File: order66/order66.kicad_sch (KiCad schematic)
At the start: 214 parts, among them J1 NICEVIEW, J2 Pouch Battery Connector, J3 swd connector, J4 3220-10-0100-00, J6 millmax connector, SW1 AUX1, SW10 Z, SW100 OFF/ON, SW11 AUX7, SW12 2, SW13 W, SW14 S, SW15 X, SW16 LALT, SW17 3, SW18 E, SW19 D, SW2 ESC, SW20 C, SW21 GUI, SW22 4, SW23 R, SW24 F, SW25 V, SW26 RAISE, SW27 5, SW28 T, SW29 G, SW3 TAB, SW30 B, SW31 LSPACE, SW32 AUX2, SW33 6, SW34 Y, SW35 H, SW36 N, SW37 RSPACE, SW38 AUX3, SW39 7, SW4 CAPSLCK, SW40 U, SW41 J, SW42 M, SW43 LOWER, SW44 AUX4, SW45 8, SW46 I, SW47 K, SW48 ,<, SW49 LEFT, SW5 LSHIFT, SW50 9, SW51 O, SW52 L, SW53 .>, SW54 DOWN, SW55 AUX5, SW56 0, SW57 P, SW58 ;:, SW59 /?, SW6 LCTRL, SW60 UP, SW61 AUX6, SW62 BACKSPACE, SW63 BACKSLASH, SW64 ENTER, SW65 RSHIFT, SW66 RIGHT, SW67 RST, SW68 OFF/ON, SW7 1, SW8 Q, SW9 A, U1 NiceNano

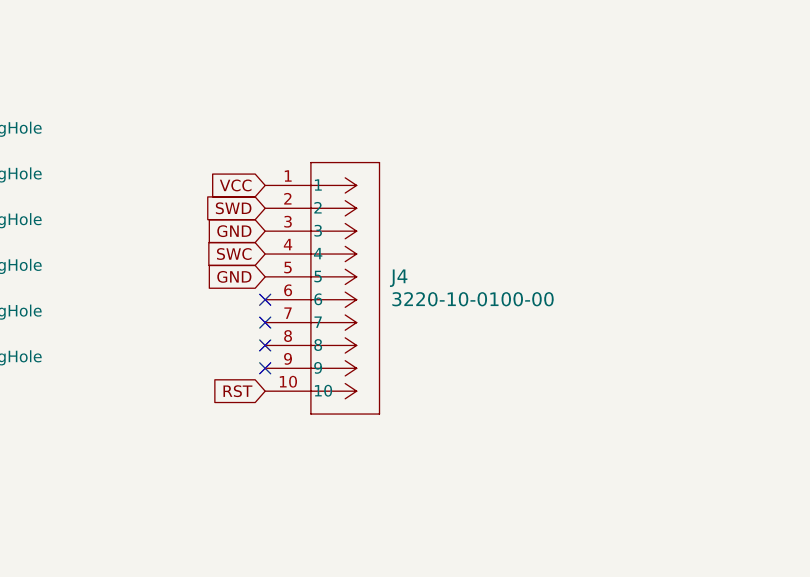
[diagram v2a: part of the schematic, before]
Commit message: removing the connector for the link for now
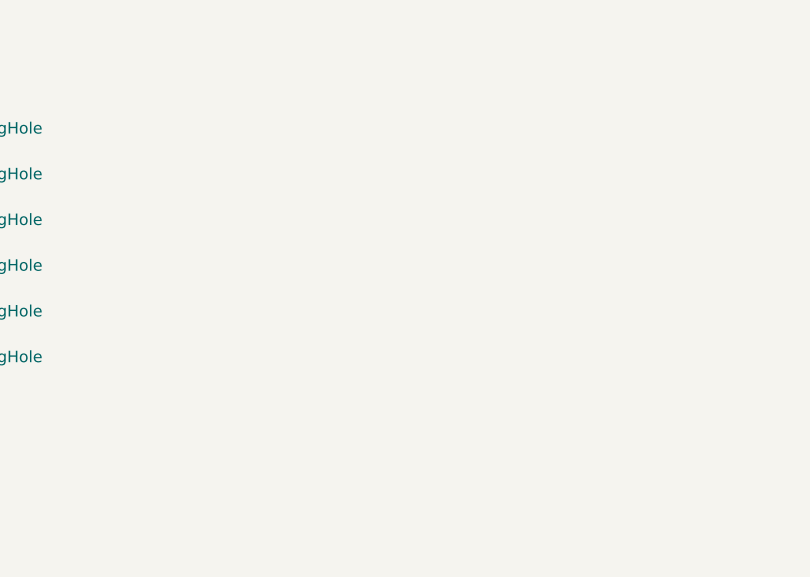
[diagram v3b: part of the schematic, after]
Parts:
- removed J4: 3220-10-0100-00, 3220_10_0100_00:CONN_3220-10-0100-00_CNC, symbol 2025-06-30_18-11-54:3220-10-0100-00
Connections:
- no-connect marks 6 -> 2
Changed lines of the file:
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@@
 	)
 	(no_connect
-		(at 152.4 158.75)
-	)
-	(no_connect
-		(at 152.4 156.21)
-	)
-	(no_connect
-		(at 152.4 161.29)
-	)
-	(no_connect
 		(at 55.88 144.78)
 	)
@@
 		(at 96.52 184.15)
 	)
-	(no_connect
-		(at 152.4 153.67)
-	)
 	(wire
 		(pts
@@
 		)
 	)
-	(global_label "SWD"
-		(shape input)
-		(at 152.4 143.51 180)
-		(fields_autoplaced yes)
-		(effects
-			(font
-				(size 1.27 1.27)
-			)
-			(justify right)
-		)
-		(property "Intersheetrefs" "${INTERSHEET_REFS}"
-			(at 145.4839 143.51 0)
-			(effects
-				(font
-					(size 1.27 1.27)
-				)
-				(justify right)
-				(hide yes)
-			)
-		)
-	)
-	(global_label "SWC"
-		(shape input)
-		(at 152.4 148.59 180)
-		(fields_autoplaced yes)
-		(effects
-			(font
-				(size 1.27 1.27)
-			)
-			(justify right)
-		)
-		(property "Intersheetrefs" "${INTERSHEET_REFS}"
-			(at 145.4839 148.59 0)
-			(effects
-				(font
-					(size 1.27 1.27)
-				)
-				(justify right)
-				(hide yes)
-			)
-		)
-	)
 	(global_label "COL10"
 		(shape input)
@@
 		)
 	)
-	(global_label "GND"
-		(shape input)
-		(at 152.4 146.05 180)
-		(fields_autoplaced yes)
-		(effects
-			(font
-				(size 1.27 1.27)
-			)
-			(justify right)
-		)
-		(property "Intersheetrefs" "${INTERSHEET_REFS}"
-			(at 145.5443 146.05 0)
-			(effects
-				(font
-					(size 1.27 1.27)
-				)
-				(justify right)
-				(hide yes)
-			)
-		)
-	)
 	(global_label "COL4"
 		(shape input)
@@
 		)
 	)
-	(global_label "GND"
-		(shape input)
-		(at 152.4 151.13 180)
-		(fields_autoplaced yes)
-		(effects
-			(font
-				(size 1.27 1.27)
-			)
-			(justify right)
-		)
-		(property "Intersheetrefs" "${INTERSHEET_REFS}"
-			(at 145.5443 151.13 0)
-			(effects
-				(font
-					(size 1.27 1.27)
-				)
-				(justify right)
-				(hide yes)
-			)
-		)
-	)
 	(global_label "VBATT+"
 		(shape input)
@@
 		)
 	)
-	(global_label "RST"
-		(shape input)
-		(at 152.4 163.83 180)
-		(fields_autoplaced yes)
-		(effects
-			(font
-				(size 1.27 1.27)
-			)
-			(justify right)
-		)
-		(property "Intersheetrefs" "${INTERSHEET_REFS}"
-			(at 145.9677 163.83 0)
-			(effects
-				(font
-					(size 1.27 1.27)
-				)
-				(justify right)
-				(hide yes)
-			)
-		)
-	)
 	(global_label "ROW0"
 		(shape input)
@@
 		)
 	)
-	(global_label "VCC"
-		(shape input)
-		(at 152.4 140.97 180)
-		(fields_autoplaced yes)
-		(effects
-			(font
-				(size 1.27 1.27)
-			)
-			(justify right)
-		)
-		(property "Intersheetrefs" "${INTERSHEET_REFS}"
-			(at 145.7862 140.97 0)
-			(effects
-				(font
-					(size 1.27 1.27)
-				)
-				(justify right)
-				(hide yes)
-			)
-		)
-	)
 	(symbol
 		(lib_id "Diode:1N4148W")
@@
 					(unit 1)
 				)
-			)
-		)
-	)
-	(symbol
-		(lib_id "2025-06-30_18-11-54:3220-10-0100-00")
-		(at 152.4 140.97 0)
-		(unit 1)
-		(exclude_from_sim no)
-		(in_bom yes)
-		(on_board yes)
-		(dnp no)
-		(property "Reference" "J4"
-			(at 166.37 151.1299 0)
-			(effects
-				(font
-					(size 1.524 1.524)
-				)
-				(justify left)
-			)
-		)
-		(property "Value" "3220-10-0100-00"
-			(at 166.37 153.6699 0)
-			(effects
-				(font
-					(size 1.524 1.524)
-				)
-				(justify left)
-			)
-		)
-		(property "Footprint" "3220_10_0100_00:CONN_3220-10-0100-00_CNC"
-			(at 152.4 140.97 0)
-			(effects
-				(font
-					(size 1.27 1.27)
-					(italic yes)
-				)
-				(hide yes)
-			)
-		)
-		(property "Datasheet" "3220-10-0100-00"
-			(at 152.4 140.97 0)
-			(effects
-				(font
-					(size 1.27 1.27)
-					(italic yes)
-				)
-				(hide yes)
-			)
-		)
-		(property "Description" ""
-			(at 152.4 140.97 0)
-			(effects
-				(font
-					(size 1.27 1.27)
-				)
-				(hide yes)
-			)
-		)
-		(pin "10"
-		)
-		(pin "6"
-		)
-		(pin "5"
-		)
-		(pin "4"
-		)
-		(pin "2"
-		)
-		(pin "9"
-		)
-		(pin "8"
-		)
-		(pin "7"
-		)
-		(pin "1"
-		)
-		(pin "3"
-		)
-		(instances
-			(project ""
-				(path "/4342f055-467b-4789-a8ed-b19f1b214d4d"
-					(reference "J4")
-					(unit 1)
-				)

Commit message: 5x12 with backlight wip
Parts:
- removed D1, D10, D11, D12, D13, D14, D15, D16, D17, D18, D19, D2, D20, D21, D22, D23, D24, D25, D26, D27, D28, D29, D3, D30, D31, D32, D33, D34, D35, D36, D37, D38, D39, D4, D40, D41, D42, D43, D44, D45, D46, D47, D48, D49, D5, D50, D51, D52, D53, D54, D55, D56, D57, D58, D59, D6, D60, D61, D62, D63, D64, D65, D66, D7, D8, D9: 1N4148, Diode_THT:D_DO-35_SOD27_P7.62mm_Horizontal, symbol Diode:1N4148
- removed D101, D102, D103, D104, D105, D106, D107, D108, D109, D110, D111, D112, D113, D114, D115, D116, D117, D118, D119, D120, D121, D122, D123, D124, D125, D126, D127, D128, D129, D130, D131, D132, D133, D134, D135, D136, D137, D138, D139, D140, D141, D142, D143, D144, D145, D146, D147, D148, D149, D150, D151, D152, D153, D154, D155, D156, D157, D158, D159, D160, D161, D162, D163, D164, D165, D166: 1N4148, Diode_SMD:D_SOD-123, symbol Diode:1N4148W
- removed SW100: OFF/ON, SSSS811101:SW_SSSS811101, symbol SSSS811101:SSSS811101
- removed SW61: AUX6, MX_Hotswap:MX-Hotswap-1U, symbol Switch:SW_Push
- removed SW62: BACKSPACE, MX_Hotswap:MX-Hotswap-1U, symbol Switch:SW_Push
- removed SW63: BACKSLASH, MX_Hotswap:MX-Hotswap-1U, symbol Switch:SW_Push
- removed SW64: ENTER, MX_Hotswap:MX-Hotswap-1U, symbol Switch:SW_Push
- removed SW65: RSHIFT, MX_Hotswap:MX-Hotswap-1U, symbol Switch:SW_Push
- removed SW66: RIGHT, MX_Hotswap:MX-Hotswap-1U, symbol Switch:SW_Push
- added D1, D10, D11, D12, D13, D14, D15, D16, D17, D18, D19, D2, D20, D21, D22, D23, D24, D25, D26, D27, D28, D29, D3, D30, D31, D32, D33, D34, D35, D36, D37, D38, D39, D4, D40, D41, D42, D43, D44, D45, D46, D47, D48, D49, D5, D50, D51, D52, D53, D54, D55, D56, D57, D58, D59, D6, D60, D7, D8, D9: 1N4148WS, Diode_SMD:D_SOD-323, symbol Diode:1N4148WS
- added D100, D101, D102, D103, D104, D105, D106, D107, D108, D109, D110, D111, D112, D113, D114, D115, D116, D117, D118, D119, D120, D61, D62, D63, D64, D65, D66, D67, D68, D69, D70, D71, D72, D73, D74, D75, D76, D77, D78, D79, D80, D81, D82, D83, D84, D85, D86, D87, D88, D89, D90, D91, D92, D93, D94, D95, D96, D97, D98, D99: WS2812B, LED_SMD:LED_WS2812B_PLCC4_5.0x5.0mm_P3.2mm, symbol LED:WS2812B
- SW1: value AUX1 -> SW_Push
- SW10: value Z -> SW_Push
- SW11: value AUX7 -> SW_Push
- SW12: value 2 -> SW_Push
- SW13: value W -> SW_Push
- SW14: value S -> SW_Push
- SW15: value X -> SW_Push
- SW16: value LALT -> SW_Push
- SW17: value 3 -> SW_Push
- SW18: value E -> SW_Push
- SW19: value D -> SW_Push
- SW2: value ESC -> SW_Push
- SW20: value C -> SW_Push
- SW21: value GUI -> SW_Push
- SW22: value 4 -> SW_Push
- SW23: value R -> SW_Push
- SW24: value F -> SW_Push
- SW25: value V -> SW_Push
- SW26: value RAISE -> SW_Push
- SW27: value 5 -> SW_Push
- SW28: value T -> SW_Push
- SW29: value G -> SW_Push
- SW3: value TAB -> SW_Push
- SW30: value B -> SW_Push
- SW31: value LSPACE -> SW_Push
- SW32: value AUX2 -> SW_Push
- SW33: value 6 -> SW_Push
- SW34: value Y -> SW_Push
- SW35: value H -> SW_Push
- SW36: value N -> SW_Push
- SW37: value RSPACE -> SW_Push
- SW38: value AUX3 -> SW_Push
- SW39: value 7 -> SW_Push
- SW4: value CAPSLCK -> SW_Push
- SW40: value U -> SW_Push
- SW41: value J -> SW_Push
- SW42: value M -> SW_Push
- SW43: value LOWER -> SW_Push
- SW44: value AUX4 -> SW_Push
- SW45: value 8 -> SW_Push
- SW46: value I -> SW_Push
- SW47: value K -> SW_Push
- SW48: value ,< -> SW_Push
- SW49: value LEFT -> SW_Push
- SW5: value LSHIFT -> SW_Push
- SW50: value 9 -> SW_Push
- SW51: value O -> SW_Push
- SW52: value L -> SW_Push
- SW53: value .> -> SW_Push
- SW54: value DOWN -> SW_Push
- SW55: value AUX5 -> SW_Push
- SW56: value 0 -> SW_Push
- SW57: value P -> SW_Push
- SW58: value ;: -> SW_Push
- SW59: value /? -> SW_Push
- SW6: value LCTRL -> SW_Push
- SW60: value UP -> SW_Push
- SW7: value 1 -> SW_Push
- SW8: value Q -> SW_Push
- SW9: value A -> SW_Push
- renumbered J6 to J4, SW67 to SW61, SW68 to SW62
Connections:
- net COL0: now also SW1.1, SW13.1, SW25.1, SW37.1, SW49.1; no longer SW1.2, SW2.2, SW3.2, SW4.2, SW5.2, SW6.2
- net COL1: now also SW14.1, SW2.1, SW26.1, SW38.1, SW50.1; no longer SW10.2, SW11.2, SW7.2, SW8.2, SW9.2
- net COL10: now also SW11.1, SW23.1, SW35.1, SW47.1, SW59.1; no longer SW55.2, SW56.2, SW57.2, SW58.2, SW59.2, SW60.2
- net COL11: now also SW12.1, SW24.1, SW36.1, SW48.1, SW60.1
- net COL2: now also SW15.1, SW27.1, SW3.1, SW39.1, SW51.1; no longer SW12.2, SW13.2, SW14.2, SW15.2, SW16.2
- net COL3: now also SW16.1, SW28.1, SW4.1, SW40.1, SW52.1; no longer SW17.2, SW18.2, SW19.2, SW20.2, SW21.2
- net COL4: now also SW17.1, SW29.1, SW41.1, SW5.1, SW53.1; no longer SW22.2, SW23.2, SW24.2, SW25.2, SW26.2
- net COL5: now also SW18.1, SW30.1, SW42.1, SW54.1, SW6.1; no longer SW27.2, SW28.2, SW29.2, SW30.2, SW31.2
- net COL6: now also SW19.1, SW31.1, SW43.1, SW55.1, SW7.1; no longer SW32.2, SW33.2, SW34.2, SW35.2, SW36.2, SW37.2
- net COL7: now also SW20.1, SW32.1, SW44.1, SW56.1, SW8.1; no longer SW38.2, SW39.2, SW40.2, SW41.2, SW42.2, SW43.2
- net COL8: now also SW21.1, SW33.1, SW45.1, SW57.1, SW9.1; no longer SW44.2, SW45.2, SW46.2, SW47.2, SW48.2, SW49.2
- net COL9: now also SW10.1, SW22.1, SW34.1, SW46.1, SW58.1; no longer SW50.2, SW51.2, SW52.2, SW53.2, SW54.2
- net GND: now also D100.1 (VDD), D101.1 (VDD), D102.1 (VDD), D103.1 (VDD), D104.1 (VDD), D105.1 (VDD), D106.1 (VDD), D107.1 (VDD), D108.1 (VDD), D109.1 (VDD), D110.1 (VDD), D111.1 (VDD), D112.1 (VDD), D113.1 (VDD), D114.1 (VDD), D115.1 (VDD), D116.1 (VDD), D117.1 (VDD), D118.1 (VDD), D119.1 (VDD), D120.1 (VDD), D61.1 (VDD), D62.1 (VDD), D63.1 (VDD), D64.1 (VDD), D65.1 (VDD), D66.1 (VDD), D67.1 (VDD), D68.1 (VDD), D69.1 (VDD), D70.1 (VDD), D71.1 (VDD), D72.1 (VDD), D73.1 (VDD), D74.1 (VDD), D75.1 (VDD), D76.1 (VDD), D77.1 (VDD), D78.1 (VDD), D79.1 (VDD), D80.1 (VDD), D81.1 (VDD), D82.1 (VDD), D83.1 (VDD), D84.1 (VDD), D85.1 (VDD), D86.1 (VDD), D87.1 (VDD), D88.1 (VDD), D89.1 (VDD), D90.1 (VDD), D91.1 (VDD), D92.1 (VDD), D93.1 (VDD), D94.1 (VDD), D95.1 (VDD), D96.1 (VDD), D97.1 (VDD), D98.1 (VDD), D99.1 (VDD)
- net ROW0: now also D1.1 (K), D10.1 (K), D11.1 (K), D12.1 (K), D2.1 (K), D3.1 (K), D4.1 (K), D5.1 (K), D6.1 (K), D7.1 (K), D8.1 (K), D9.1 (K)
- net ROW1: now also D13.1 (K), D14.1 (K), D15.1 (K), D16.1 (K), D17.1 (K), D18.1 (K), D19.1 (K), D20.1 (K), D21.1 (K), D22.1 (K), D23.1 (K), D24.1 (K)
- net ROW2: now also D25.1 (K), D26.1 (K), D27.1 (K), D28.1 (K), D29.1 (K), D30.1 (K), D31.1 (K), D32.1 (K), D33.1 (K), D34.1 (K), D35.1 (K), D36.1 (K)
- net ROW3: now also D37.1 (K), D38.1 (K), D39.1 (K), D40.1 (K), D41.1 (K), D42.1 (K), D43.1 (K), D44.1 (K), D45.1 (K), D46.1 (K), D47.1 (K), D48.1 (K)
- net ROW4: now also D49.1 (K), D50.1 (K), D51.1 (K), D52.1 (K), D53.1 (K), D54.1 (K), D55.1 (K), D56.1 (K), D57.1 (K), D58.1 (K), D59.1 (K), D60.1 (K)
- net VCC: now also D100.3 (VSS), D101.3 (VSS), D102.3 (VSS), D103.3 (VSS), D104.3 (VSS), D105.3 (VSS), D106.3 (VSS), D107.3 (VSS), D108.3 (VSS), D109.3 (VSS), D110.3 (VSS), D111.3 (VSS), D112.3 (VSS), D113.3 (VSS), D114.3 (VSS), D115.3 (VSS), D116.3 (VSS), D117.3 (VSS), D118.3 (VSS), D119.3 (VSS), D120.3 (VSS), D61.3 (VSS), D62.3 (VSS), D63.3 (VSS), D64.3 (VSS), D65.3 (VSS), D66.3 (VSS), D67.3 (VSS), D68.3 (VSS), D69.3 (VSS), D70.3 (VSS), D71.3 (VSS), D72.3 (VSS), D73.3 (VSS), D74.3 (VSS), D75.3 (VSS), D76.3 (VSS), D77.3 (VSS), D78.3 (VSS), D79.3 (VSS), D80.3 (VSS), D81.3 (VSS), D82.3 (VSS), D83.3 (VSS), D84.3 (VSS), D85.3 (VSS), D86.3 (VSS), D87.3 (VSS), D88.3 (VSS), D89.3 (VSS), D90.3 (VSS), D91.3 (VSS), D92.3 (VSS), D93.3 (VSS), D94.3 (VSS), D95.3 (VSS), D96.3 (VSS), D97.3 (VSS), D98.3 (VSS), D99.3 (VSS)
- net ROW5 renamed BCKLT
- net BCKLT: now also D61.4 (DIN)
- new net: D27.2 (A), SW27.2
- new net: D62.2 (DOUT), D63.4 (DIN)
- new net: D61.2 (DOUT), D62.4 (DIN)
- new net: D40.2 (A), SW40.2
- new net: D17.2 (A), SW17.2
- new net: D32.2 (A), SW32.2
- new net: D57.2 (A), SW57.2
- new net: D39.2 (A), SW39.2
- new net: D11.2 (A), SW11.2
- new net: D49.2 (A), SW49.2
- new net: D4.2 (A), SW4.2
- new net: D100.2 (DOUT), D99.4 (DIN)
- new net: D100.4 (DIN), D101.2 (DOUT)
- new net: D101.4 (DIN), D102.2 (DOUT)
- new net: D119.2 (DOUT), D120.4 (DIN)
- new net: D108.4 (DIN), D96.2 (DOUT)
- new net: D95.2 (DOUT), D96.4 (DIN)
- new net: D64.2 (DOUT), D65.4 (DIN)
- new net: D63.2 (DOUT), D64.4 (DIN)
- new net: D68.2 (DOUT), D69.4 (DIN)
- new net: D67.2 (DOUT), D68.4 (DIN)
- new net: D45.2 (A), SW45.2
- new net: D118.2 (DOUT), D119.4 (DIN)
- new net: D117.2 (DOUT), D118.4 (DIN)
- new net: D37.2 (A), SW37.2
- new net: D10.2 (A), SW10.2
- new net: D109.2 (DOUT), D110.4 (DIN)
- new net: D109.4 (DIN), D97.2 (DOUT)
- new net: D35.2 (A), SW35.2
- new net: D53.2 (A), SW53.2
- new net: D78.4 (DIN), D79.2 (DOUT)
- new net: D79.4 (DIN), D80.2 (DOUT)
- new net: D48.2 (A), SW48.2
- new net: D93.2 (DOUT), D94.4 (DIN)
- new net: D92.2 (DOUT), D93.4 (DIN)
- new net: D58.2 (A), SW58.2
- new net: D88.2 (DOUT), D89.4 (DIN)
- new net: D87.2 (DOUT), D88.4 (DIN)
- new net: D22.2 (A), SW22.2
- new net: D55.2 (A), SW55.2
- new net: D24.2 (A), SW24.2
- new net: D73.2 (DOUT), D85.4 (DIN)
- new net: D73.4 (DIN), D74.2 (DOUT)
- new net: D21.2 (A), SW21.2
- new net: D105.4 (DIN), D106.2 (DOUT)
- new net: D106.4 (DIN), D107.2 (DOUT)
- new net: D6.2 (A), SW6.2
- new net: D3.2 (A), SW3.2
- new net: D44.2 (A), SW44.2
- new net: D112.2 (DOUT), D113.4 (DIN)
- new net: D111.2 (DOUT), D112.4 (DIN)
- new net: D26.2 (A), SW26.2
- new net: D86.2 (DOUT), D87.4 (DIN)
- new net: D60.2 (A), SW60.2
- new net: D47.2 (A), SW47.2
- new net: D80.4 (DIN), D81.2 (DOUT)
- new net: D81.4 (DIN), D82.2 (DOUT)
- new net: D25.2 (A), SW25.2
- new net: D113.2 (DOUT), D114.4 (DIN)
- new net: D28.2 (A), SW28.2
- new net: D52.2 (A), SW52.2
- new net: D50.2 (A), SW50.2
- new net: D9.2 (A), SW9.2
- new net: D14.2 (A), SW14.2
- new net: D91.2 (DOUT), D92.4 (DIN)
- new net: D16.2 (A), SW16.2
- new net: D13.2 (A), SW13.2
- new net: D115.2 (DOUT), D116.4 (DIN)
- new net: D114.2 (DOUT), D115.4 (DIN)
- new net: D30.2 (A), SW30.2
- new net: D116.2 (DOUT), D117.4 (DIN)
- new net: D66.2 (DOUT), D67.4 (DIN)
- new net: D65.2 (DOUT), D66.4 (DIN)
- new net: D46.2 (A), SW46.2
- new net: D72.2 (DOUT), D84.4 (DIN)
- new net: D71.2 (DOUT), D72.4 (DIN)
- new net: D15.2 (A), SW15.2
- new net: D33.2 (A), SW33.2
- new net: D103.4 (DIN), D104.2 (DOUT)
- new net: D104.4 (DIN), D105.2 (DOUT)
- new net: D38.2 (A), SW38.2
- new net: D12.2 (A), SW12.2
- new net: D19.2 (A), SW19.2
- new net: D54.2 (A), SW54.2
- new net: D18.2 (A), SW18.2
- new net: D29.2 (A), SW29.2
- new net: D102.4 (DIN), D103.2 (DOUT)
- new net: D23.2 (A), SW23.2
- new net: D41.2 (A), SW41.2
- new net: D98.4 (DIN), D99.2 (DOUT)
- new net: D7.2 (A), SW7.2
- new net: D107.4 (DIN), D108.2 (DOUT)
- new net: D94.2 (DOUT), D95.4 (DIN)
- new net: D74.4 (DIN), D75.2 (DOUT)
- new net: D90.2 (DOUT), D91.4 (DIN)
- new net: D89.2 (DOUT), D90.4 (DIN)
- new net: D2.2 (A), SW2.2
- new net: D43.2 (A), SW43.2
- new net: D97.4 (DIN), D98.2 (DOUT)
- new net: D70.2 (DOUT), D71.4 (DIN)
- new net: D20.2 (A), SW20.2
- new net: D51.2 (A), SW51.2
- new net: D56.2 (A), SW56.2
- new net: D36.2 (A), SW36.2
- new net: D75.4 (DIN), D76.2 (DOUT)
- new net: D76.4 (DIN), D77.2 (DOUT)
- new net: D8.2 (A), SW8.2
- new net: D77.4 (DIN), D78.2 (DOUT)
- new net: D110.2 (DOUT), D111.4 (DIN)
- new net: D34.2 (A), SW34.2
- new net: D31.2 (A), SW31.2
- new net: D5.2 (A), SW5.2
- new net: D42.2 (A), SW42.2
- new net: D83.4 (DIN), D84.2 (DOUT)
- new net: D1.2 (A), SW1.2
- new net: D59.2 (A), SW59.2
- new net: D82.4 (DIN), D83.2 (DOUT)
- new net: D69.2 (DOUT), D70.4 (DIN)
- new net: D85.2 (DOUT), D86.4 (DIN)
- no-connect marks 2 -> 1
